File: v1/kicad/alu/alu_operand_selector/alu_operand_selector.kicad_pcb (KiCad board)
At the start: 2 copper layers, 166 x 91 mm, 19 parts, among them J1 LNCPU ALU Operand Selector so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, J10 OP_{out}, J2 A_{in}, J3 B_{in}, J4 C_{in}, J5 D_{in}, J6 E_{in}, J7 F_{in}, J8 G_{in}, J9 H_{in}, U1 74HC138, U2 74LS244, U3 74HC244, U4 74HC244, U5 74HC244, U6 74HC244, U7 74HC244, U8 74HC244, U9 74HC244

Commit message: partial
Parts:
- removed J1: LNCPU ALU Operand Selector socket, male, Connector_PinHeader_2.54mm:PinHeader_1x08_P2.54mm_Horizontal
- added U10: LNCPU Type C Connector, lncpu:LNCPU_Type_C_Header, F.Cu at (54.7, 75.4)
- U1: footprint Package_DIP:DIP-16_W7.62mm -> Package_DIP:DIP-16_W7.62mm_LongPads
- U2, U3, U4, U5, U6, U7, U8, U9: footprint Package_DIP:DIP-20_W7.62mm -> Package_DIP:DIP-20_W7.62mm_LongPads
- moved U1 11.5 mm to (65.6, 69.8)
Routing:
- net /OP_{out}5: track 320.6 -> 503.8 mm, vias 9 -> 10
- net Net-(J7-D4): track 45.5 -> 186.6 mm, vias 0 -> 2
- net /OP_{out}7: track 342.0 -> 457.8 mm, vias 9 -> 11
- net /EN.C: track 197.9 -> 84.0 mm, vias 6 -> 4
- net /OP_{out}2: track 311.4 -> 407.6 mm, vias 11 -> 10
- net /OP_{out}4: track 287.1 -> 380.0 mm, vias 7 -> 10
- net /OP_{out}0: track 294.9 -> 372.4 mm, vias 8 -> 11
- net /OP_{out}3: track 295.9 -> 370.0 mm, vias 9 -> 10
- net Net-(U1-VCC): track 364.0 -> 432.3 mm, vias 10 -> 9
- net /OP_{out}6: track 321.8 -> 384.8 mm, vias 9 -> 12
- net Net-(J2-D1): track 32.4 -> 93.1 mm, vias 0 -> 6
- net Net-(J2-D3): track 95.0 -> 38.0 mm, vias 2 -> 0
- net Net-(U1-GND): track 337.4 -> 377.2 mm, vias 9 -> 11
- net Net-(J8-D6): track 72.2 -> 33.2 mm
- net Net-(U1-A0): track 9.02 -> 42.4 mm, vias 0 -> 2
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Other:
- board size 166 x 91 mm -> 163.5 x 91 mm

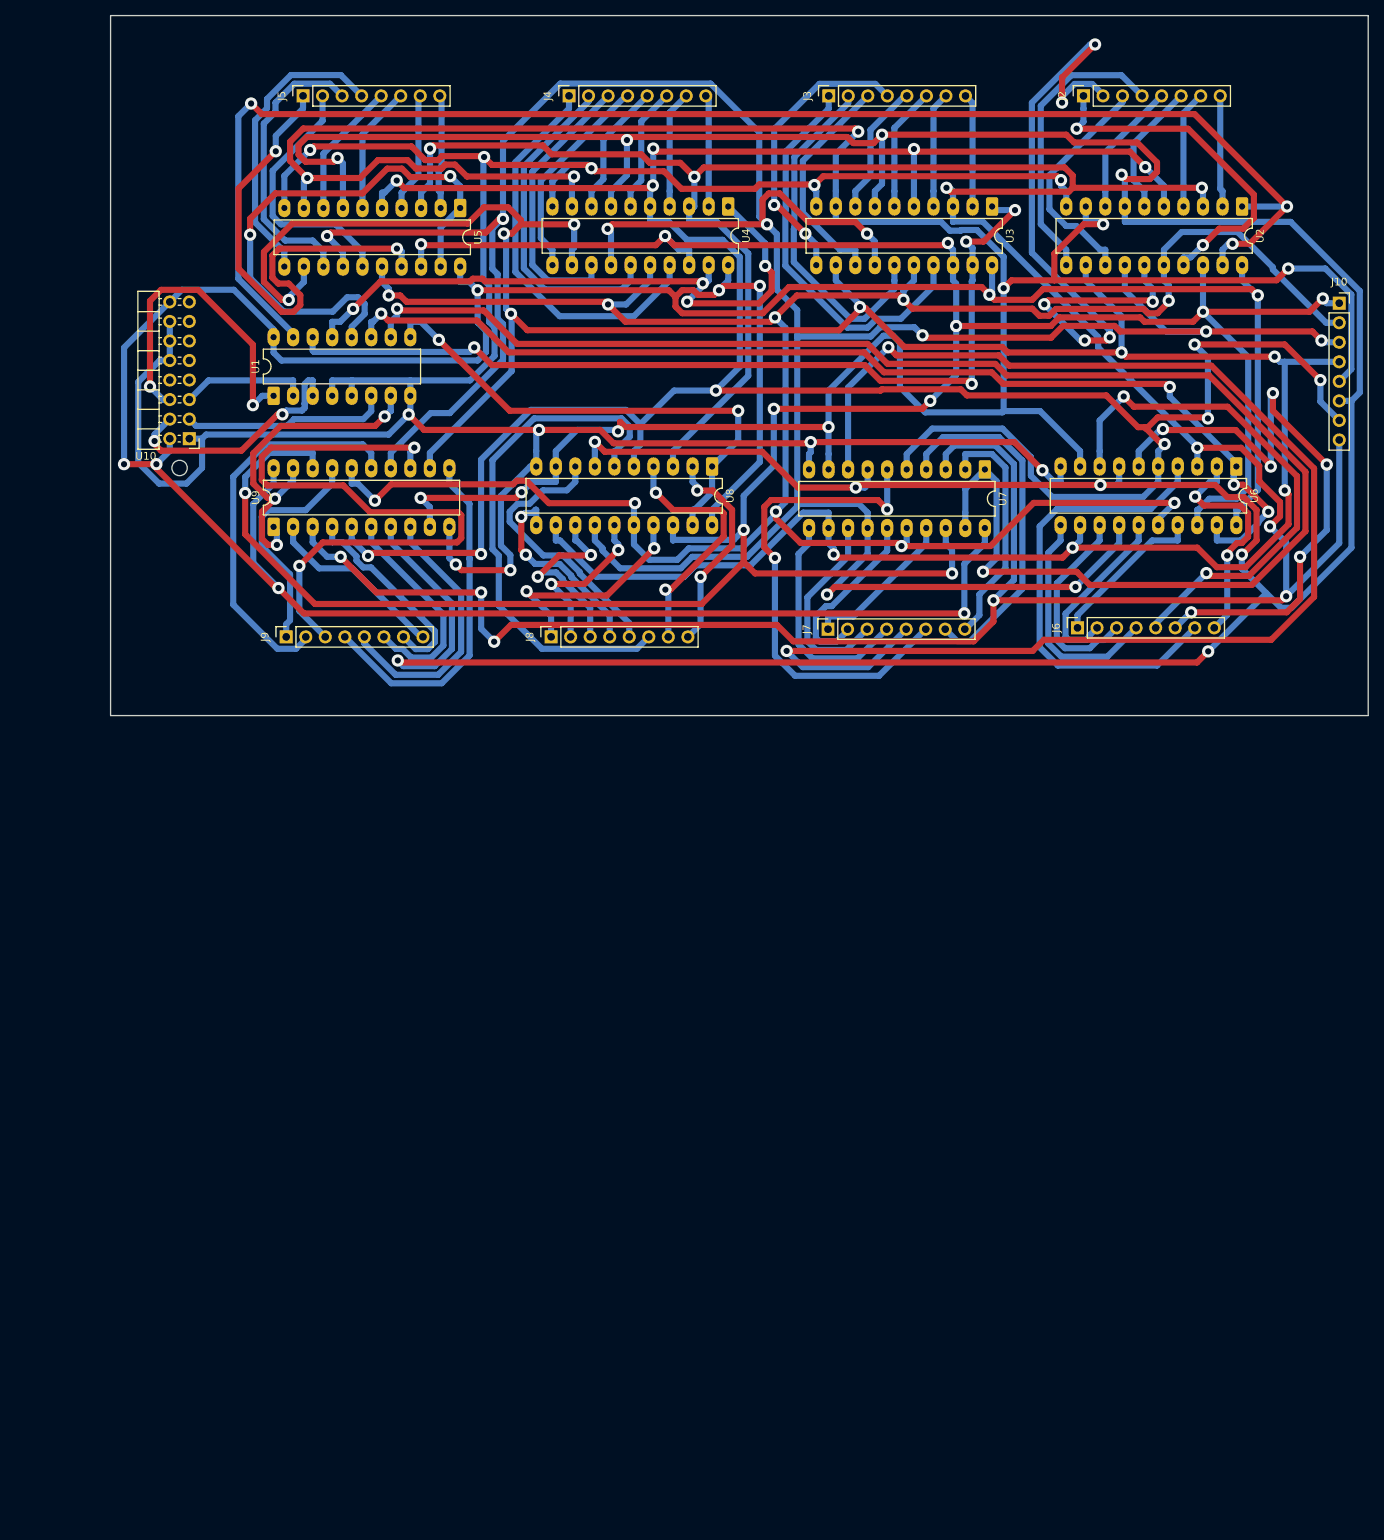
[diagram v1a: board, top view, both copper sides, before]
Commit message: readapt designs for BR, SP, SR, ALU
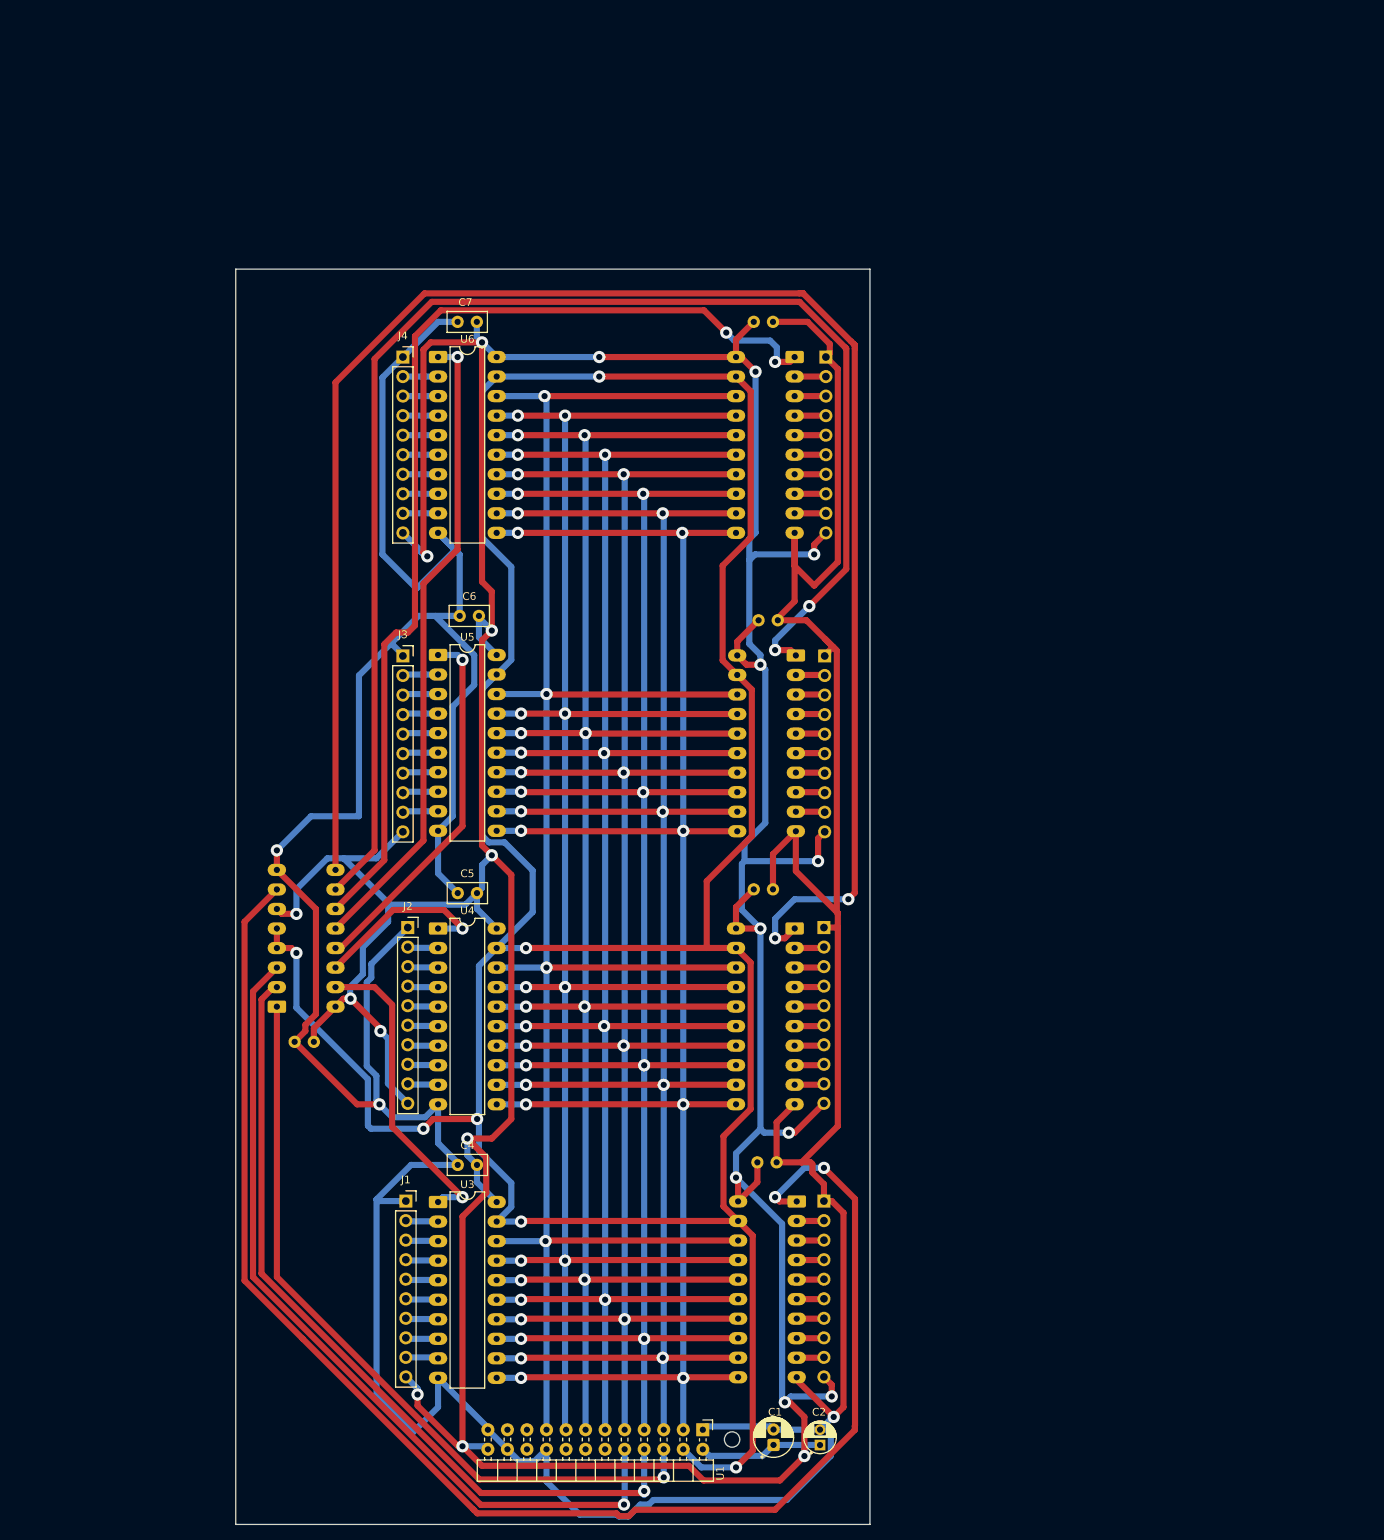
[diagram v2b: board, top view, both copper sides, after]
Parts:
- removed J10: OP_{out}, Connector_PinSocket_2.54mm:PinSocket_1x08_P2.54mm_Vertical
- removed J9: H_{in}, Connector_PinSocket_2.54mm:PinSocket_1x08_P2.54mm_Vertical
- added C1: 47u, Capacitor_THT:CP_Radial_D5.0mm_P2.00mm, F.Cu at (130.6, 206.2)
- added C10: 220n, Capacitor_THT:C_Disc_D5.0mm_W2.5mm_P2.50mm, B.Cu at (128.0, 134.0)
- added C11: 220n, Capacitor_THT:C_Disc_D5.0mm_W2.5mm_P2.50mm, B.Cu at (128.5, 169.5)
- added C2: 1u, lncpu:CP_Radial_D4.0mm_P2.00mm-Large-Holes, F.Cu at (136.7, 206.2)
- added C3: 100n, Capacitor_THT:C_Disc_D5.0mm_W2.5mm_P2.50mm, B.Cu at (70.8, 153.8)
- added C4: 220n, Capacitor_THT:C_Disc_D5.0mm_W2.5mm_P2.50mm, F.Cu at (92.1, 169.8)
- added C5: 220n, Capacitor_THT:C_Disc_D5.0mm_W2.5mm_P2.50mm, F.Cu at (92.1, 134.5)
- added C6: 220n, Capacitor_THT:C_Disc_D5.0mm_W2.5mm_P2.50mm, F.Cu at (92.3, 98.4)
- added C7: 220n, Capacitor_THT:C_Disc_D5.0mm_W2.5mm_P2.50mm, F.Cu at (92.0, 60.2)
- added C8: 220n, Capacitor_THT:C_Disc_D5.0mm_W2.5mm_P2.50mm, B.Cu at (128.0, 60.2)
- added C9: 220n, Capacitor_THT:C_Disc_D5.0mm_W2.5mm_P2.50mm, B.Cu at (128.7, 99.0)
- added J1: A_{in}, Connector_PinSocket_2.54mm:PinSocket_1x10_P2.54mm_Vertical, F.Cu at (82.8, 174.5)
- J2: value A_{in} -> B_{in}; footprint Connector_PinSocket_2.54mm:PinSocket_1x08_P2.54mm_Vertical -> Connector_PinSocket_2.54mm:PinSocket_1x10_P2.54mm_Vertical
- J3: value B_{in} -> C_{in}; footprint Connector_PinSocket_2.54mm:PinSocket_1x08_P2.54mm_Vertical -> Connector_PinSocket_2.54mm:PinSocket_1x10_P2.54mm_Vertical
- J4: value C_{in} -> D_{in}; footprint Connector_PinSocket_2.54mm:PinSocket_1x08_P2.54mm_Vertical -> Connector_PinSocket_2.54mm:PinSocket_1x10_P2.54mm_Vertical
- J5: value D_{in} -> E_{in}; footprint Connector_PinSocket_2.54mm:PinSocket_1x08_P2.54mm_Vertical -> Connector_PinSocket_2.54mm:PinSocket_1x10_P2.54mm_Vertical; moved to B.Cu
- J6: value E_{in} -> F_{in}; footprint Connector_PinSocket_2.54mm:PinSocket_1x08_P2.54mm_Vertical -> Connector_PinSocket_2.54mm:PinSocket_1x10_P2.54mm_Vertical; moved to B.Cu
- J7: value F_{in} -> G_{in}; footprint Connector_PinSocket_2.54mm:PinSocket_1x08_P2.54mm_Vertical -> Connector_PinSocket_2.54mm:PinSocket_1x10_P2.54mm_Vertical; moved to B.Cu
- J8: value G_{in} -> H_{in}; footprint Connector_PinSocket_2.54mm:PinSocket_1x08_P2.54mm_Vertical -> Connector_PinSocket_2.54mm:PinSocket_1x10_P2.54mm_Vertical; moved to B.Cu
- U1: value 74HC138 -> LNCPU Type B Header; footprint Package_DIP:DIP-16_W7.62mm_LongPads -> lncpu:LNCPU_Type_B_Header
- U10: value LNCPU Type C Connector -> 74HCT541; footprint lncpu:LNCPU_Type_C_Header -> Package_DIP:DIP-20_W7.62mm_LongPads; moved to B.Cu
- U2: value 74LS244 -> 74HC138; footprint Package_DIP:DIP-20_W7.62mm_LongPads -> Package_DIP:DIP-16_W7.62mm_LongPads; moved to B.Cu
- U3, U4, U5, U6: value 74HC244 -> 74HCT541
- U7, U8, U9: value 74HC244 -> 74HCT541; moved to B.Cu
- moved U2 163.0 mm to (66.0, 149.2), turned to 0 degrees
- moved U3 148.1 mm to (87.0, 174.6), turned to 0 degrees
- moved U1 145.5 mm to (121.4, 204.2), turned to -90 degrees
- moved J2 139.3 mm to (83.1, 138.9), turned to 0 degrees
- moved U10 126.8 mm to (133.6, 174.5)
- moved U6 104.8 mm to (87.0, 64.8), turned to 0 degrees
- moved U4 101.2 mm to (87.0, 139.1), turned to 0 degrees
- moved J3 91.5 mm to (82.4, 103.6), turned to 0 degrees
- moved U9 85.5 mm to (133.3, 139.1), turned to 180 degrees
- moved J8 81.5 mm to (137.2, 174.5), turned to 180 degrees
- moved J5 76.0 mm to (137.4, 64.8), turned to 180 degrees
- moved U5 58.2 mm to (87.0, 103.5), turned to 0 degrees
- moved J4 40.2 mm to (82.4, 64.8), turned to 0 degrees
- moved J7 38.8 mm to (137.2, 138.9), turned to 180 degrees
- moved J6 33.1 mm to (137.3, 103.6), turned to 180 degrees
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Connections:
- J2 pad 1: Net-(J2-D0) -> Net-(J1-GND)
- J2 pad 2: Net-(J2-D1) -> Net-(J2-D0)
- J2 pad 3: Net-(J2-D2) -> Net-(J2-D1)
- J2 pad 4: Net-(J2-D3) -> Net-(J2-D2)
- J2 pad 5: Net-(J2-D4) -> Net-(J2-D3)
- J2 pad 6: Net-(J2-D5) -> Net-(J2-D4)
- J2 pad 7: Net-(J2-D6) -> Net-(J2-D5)
- J2 pad 8: Net-(J2-D7) -> Net-(J2-D6)
- J3 pad 1: Net-(J3-D0) -> Net-(J1-GND)
- J3 pad 2: Net-(J3-D1) -> Net-(J3-D0)
- J3 pad 3: Net-(J3-D2) -> Net-(J3-D1)
- J3 pad 4: Net-(J3-D3) -> Net-(J3-D2)
- J3 pad 5: Net-(J3-D4) -> Net-(J3-D3)
- J3 pad 6: Net-(J3-D5) -> Net-(J3-D4)
- J3 pad 7: Net-(J3-D6) -> Net-(J3-D5)
- J3 pad 8: Net-(J3-D7) -> Net-(J3-D6)
- J4 pad 1: Net-(J4-D0) -> Net-(J1-GND)
- J4 pad 2: Net-(J4-D1) -> Net-(J4-D0)
- J4 pad 3: Net-(J4-D2) -> Net-(J4-D1)
- J4 pad 4: Net-(J4-D3) -> Net-(J4-D2)
- J4 pad 5: Net-(J4-D4) -> Net-(J4-D3)
- J4 pad 6: Net-(J4-D5) -> Net-(J4-D4)
- J4 pad 7: Net-(J4-D6) -> Net-(J4-D5)
- J4 pad 8: Net-(J4-D7) -> Net-(J4-D6)
- J5 pad 1: Net-(J5-D0) -> Net-(J1-GND)
- J5 pad 2: Net-(J5-D1) -> Net-(J5-D0)
- J5 pad 3: Net-(J5-D2) -> Net-(J5-D1)
- J5 pad 4: Net-(J5-D3) -> Net-(J5-D2)
- J5 pad 5: Net-(J5-D4) -> Net-(J5-D3)
- J5 pad 6: Net-(J5-D5) -> Net-(J5-D4)
- J5 pad 7: Net-(J5-D6) -> Net-(J5-D5)
- J5 pad 8: Net-(J5-D7) -> Net-(J5-D6)
- J6 pad 1: Net-(J6-D0) -> Net-(J1-GND)
- J6 pad 2: Net-(J6-D1) -> Net-(J6-D0)
- J6 pad 3: Net-(J6-D2) -> Net-(J6-D1)
- J6 pad 4: Net-(J6-D3) -> Net-(J6-D2)
- J6 pad 5: Net-(J6-D4) -> Net-(J6-D3)
- J6 pad 6: Net-(J6-D5) -> Net-(J6-D4)
- J6 pad 7: Net-(J6-D6) -> Net-(J6-D5)
- J6 pad 8: Net-(J6-D7) -> Net-(J6-D6)
- J7 pad 1: Net-(J7-D0) -> Net-(J1-GND)
- J7 pad 2: Net-(J7-D1) -> Net-(J7-D0)
- J7 pad 3: Net-(J7-D2) -> Net-(J7-D1)
- J7 pad 4: Net-(J7-D3) -> Net-(J7-D2)
- J7 pad 5: Net-(J7-D4) -> Net-(J7-D3)
- J7 pad 6: Net-(J7-D5) -> Net-(J7-D4)
- J7 pad 7: Net-(J7-D6) -> Net-(J7-D5)
- J7 pad 8: Net-(J7-D7) -> Net-(J7-D6)
- J8 pad 1: Net-(J8-D0) -> Net-(J1-GND)
- J8 pad 2: Net-(J8-D1) -> Net-(J8-D0)
- J8 pad 3: Net-(J8-D2) -> Net-(J8-D1)
- J8 pad 4: Net-(J8-D3) -> Net-(J8-D2)
- J8 pad 5: Net-(J8-D4) -> Net-(J8-D3)
- J8 pad 6: Net-(J8-D5) -> Net-(J8-D4)
- J8 pad 7: Net-(J8-D6) -> Net-(J8-D5)
- J8 pad 8: Net-(J8-D7) -> Net-(J8-D6)
- U1 pad 1: Net-(U1-A0) -> Net-(J1-GND)
- U1 pad 10: /EN.F -> Net-(U1-CTRL_{3})
- U1 pad 11: /EN.E -> /OP_{out}3
- U1 pad 12: /EN.D -> unconnected-(U1-CTRL_{4}-Pad12)
- U1 pad 13: /EN.C -> /OP_{out}2
- U1 pad 14: /EN.B -> unconnected-(U1-CTRL_{5}-Pad14)
- U1 pad 15: /EN.A -> /OP_{out}1
- U1 pad 16: Net-(U1-VCC) -> unconnected-(U1-CTRL_{6}-Pad16)
- U1 pad 2: Net-(U1-A1) -> Net-(J1-VCC)
- U1 pad 3: Net-(U1-A2) -> /OP_{out}7
- U1 pad 4: Net-(U1-GND) -> /~{EN}
- U1 pad 5: Net-(U1-GND) -> /OP_{out}6
- U1 pad 6: Net-(U1-E3) -> Net-(U1-CTRL_{1})
- U1 pad 7: /EN.H -> /OP_{out}5
- U1 pad 8: Net-(U1-GND) -> Net-(U1-CTRL_{2})
- U1 pad 9: /EN.G -> /OP_{out}4
- U10 pad 1: Net-(U1-GND) -> /EN.H
- U10 pad 10: Net-(U1-GND) -> Net-(J1-GND)
- U10 pad 11: unconnected-(U10-RST-Pad11) -> /OP_{out}7
- U10 pad 12: Net-(U1-GND) -> /OP_{out}6
- U10 pad 13: unconnected-(U10-CLK1-Pad13) -> /OP_{out}5
- U10 pad 14: Net-(U1-GND) -> /OP_{out}4
- U10 pad 15: unconnected-(U10-CLK2-Pad15) -> /OP_{out}3
- U10 pad 16: Net-(U1-VCC) -> /OP_{out}2
- U10 pad 2: Net-(U1-VCC) -> Net-(J8-D0)
- U10 pad 3: Net-(U1-E3) -> Net-(J8-D1)
- U10 pad 4: Net-(U1-A2) -> Net-(J8-D2)
- U10 pad 5: Net-(U1-A1) -> Net-(J8-D3)
- U10 pad 6: Net-(U1-A0) -> Net-(J8-D4)
- U10 pad 7: unconnected-(U10-CTRL_{4}-Pad7) -> Net-(J8-D5)
- U10 pad 8: unconnected-(U10-CTRL_{5}-Pad8) -> Net-(J8-D6)
- U10 pad 9: unconnected-(U10-CTRL_{6}-Pad9) -> Net-(J8-D7)
- U2 pad 1: /EN.A -> Net-(U1-CTRL_{1})
- U2 pad 10: Net-(U1-GND) -> /EN.F
- U2 pad 11: Net-(J2-D3) -> /EN.E
- U2 pad 12: /OP_{out}3 -> /EN.D
- U2 pad 13: Net-(J2-D2) -> /EN.C
- U2 pad 14: /OP_{out}2 -> /EN.B
- U2 pad 15: Net-(J2-D1) -> /EN.A
- U2 pad 16: /OP_{out}1 -> Net-(J1-VCC)
- U2 pad 2: Net-(J2-D7) -> Net-(U1-CTRL_{2})
- U2 pad 3: /OP_{out}7 -> Net-(U1-CTRL_{3})
- U2 pad 4: Net-(J2-D6) -> /~{EN}
- U2 pad 5: /OP_{out}6 -> /~{EN}
- U2 pad 6: Net-(J2-D5) -> Net-(J1-VCC)
- U2 pad 7: /OP_{out}5 -> /EN.H
- U2 pad 8: Net-(J2-D4) -> Net-(J1-GND)
- U2 pad 9: /OP_{out}4 -> /EN.G
- U3 pad 1: /EN.B -> /EN.A
- U3 pad 10: Net-(U1-GND) -> Net-(J1-GND)
- U3 pad 11: Net-(J3-D3) -> /OP_{out}7
- U3 pad 12: /OP_{out}3 -> /OP_{out}6
- U3 pad 13: Net-(J3-D2) -> /OP_{out}5
- U3 pad 14: /OP_{out}2 -> /OP_{out}4
- U3 pad 15: Net-(J3-D1) -> /OP_{out}3
- U3 pad 16: /OP_{out}1 -> /OP_{out}2
- U3 pad 17: Net-(J3-D0) -> /OP_{out}1
- U3 pad 19: /EN.B -> /~{EN}
- U3 pad 2: Net-(J3-D7) -> Net-(J1-D0)
- U3 pad 20: Net-(U1-VCC) -> Net-(J1-VCC)
- U3 pad 3: /OP_{out}7 -> Net-(J1-D1)
- U3 pad 4: Net-(J3-D6) -> Net-(J1-D2)
- U3 pad 5: /OP_{out}6 -> Net-(J1-D3)
- U3 pad 6: Net-(J3-D5) -> Net-(J1-D4)
- U3 pad 7: /OP_{out}5 -> Net-(J1-D5)
- U3 pad 8: Net-(J3-D4) -> Net-(J1-D6)
- U3 pad 9: /OP_{out}4 -> Net-(J1-D7)
- U4 pad 1: /EN.C -> /EN.B
- U4 pad 10: Net-(U1-GND) -> Net-(J1-GND)
- U4 pad 11: Net-(J4-D3) -> /OP_{out}7
- U4 pad 12: /OP_{out}3 -> /OP_{out}6
- U4 pad 13: Net-(J4-D2) -> /OP_{out}5
- U4 pad 14: /OP_{out}2 -> /OP_{out}4
- U4 pad 15: Net-(J4-D1) -> /OP_{out}3
- U4 pad 16: /OP_{out}1 -> /OP_{out}2
- U4 pad 17: Net-(J4-D0) -> /OP_{out}1
- U4 pad 19: /EN.C -> /~{EN}
- U4 pad 2: Net-(J4-D7) -> Net-(J2-D0)
- U4 pad 20: Net-(U1-VCC) -> Net-(J1-VCC)
- U4 pad 3: /OP_{out}7 -> Net-(J2-D1)
- U4 pad 4: Net-(J4-D6) -> Net-(J2-D2)
- U4 pad 5: /OP_{out}6 -> Net-(J2-D3)
- U4 pad 6: Net-(J4-D5) -> Net-(J2-D4)
- U4 pad 7: /OP_{out}5 -> Net-(J2-D5)
- U4 pad 8: Net-(J4-D4) -> Net-(J2-D6)
- U4 pad 9: /OP_{out}4 -> Net-(J2-D7)
- U5 pad 1: /EN.D -> /EN.C
- U5 pad 10: Net-(U1-GND) -> Net-(J1-GND)
- U5 pad 11: Net-(J5-D3) -> /OP_{out}7
- U5 pad 12: /OP_{out}3 -> /OP_{out}6
- U5 pad 13: Net-(J5-D2) -> /OP_{out}5
- U5 pad 14: /OP_{out}2 -> /OP_{out}4
- U5 pad 15: Net-(J5-D1) -> /OP_{out}3
- U5 pad 16: /OP_{out}1 -> /OP_{out}2
- U5 pad 17: Net-(J5-D0) -> /OP_{out}1
- U5 pad 19: /EN.D -> /~{EN}
- U5 pad 2: Net-(J5-D7) -> Net-(J3-D0)
- U5 pad 20: Net-(U1-VCC) -> Net-(J1-VCC)
- U5 pad 3: /OP_{out}7 -> Net-(J3-D1)
- U5 pad 4: Net-(J5-D6) -> Net-(J3-D2)
- U5 pad 5: /OP_{out}6 -> Net-(J3-D3)
- U5 pad 6: Net-(J5-D5) -> Net-(J3-D4)
- U5 pad 7: /OP_{out}5 -> Net-(J3-D5)
- U5 pad 8: Net-(J5-D4) -> Net-(J3-D6)
- U5 pad 9: /OP_{out}4 -> Net-(J3-D7)
- U6 pad 1: /EN.E -> /EN.D
- U6 pad 10: Net-(U1-GND) -> Net-(J1-GND)
- U6 pad 11: Net-(J6-D3) -> /OP_{out}7
- U6 pad 12: /OP_{out}3 -> /OP_{out}6
- U6 pad 13: Net-(J6-D2) -> /OP_{out}5
- U6 pad 14: /OP_{out}2 -> /OP_{out}4
- U6 pad 15: Net-(J6-D1) -> /OP_{out}3
- U6 pad 16: /OP_{out}1 -> /OP_{out}2
- U6 pad 17: Net-(J6-D0) -> /OP_{out}1
- U6 pad 19: /EN.E -> /~{EN}
- U6 pad 2: Net-(J6-D7) -> Net-(J4-D0)
- U6 pad 20: Net-(U1-VCC) -> Net-(J1-VCC)
- U6 pad 3: /OP_{out}7 -> Net-(J4-D1)
- U6 pad 4: Net-(J6-D6) -> Net-(J4-D2)
- U6 pad 5: /OP_{out}6 -> Net-(J4-D3)
- U6 pad 6: Net-(J6-D5) -> Net-(J4-D4)
- U6 pad 7: /OP_{out}5 -> Net-(J4-D5)
- U6 pad 8: Net-(J6-D4) -> Net-(J4-D6)
- U6 pad 9: /OP_{out}4 -> Net-(J4-D7)
- U7 pad 1: /EN.F -> /EN.E
- U7 pad 10: Net-(U1-GND) -> Net-(J1-GND)
- U7 pad 11: Net-(J7-D3) -> /OP_{out}7
- U7 pad 12: /OP_{out}3 -> /OP_{out}6
- U7 pad 13: Net-(J7-D2) -> /OP_{out}5
- U7 pad 14: /OP_{out}2 -> /OP_{out}4
- U7 pad 15: Net-(J7-D1) -> /OP_{out}3
- U7 pad 16: /OP_{out}1 -> /OP_{out}2
- U7 pad 17: Net-(J7-D0) -> /OP_{out}1
- U7 pad 19: /EN.F -> /~{EN}
- U7 pad 2: Net-(J7-D7) -> Net-(J5-D0)
- U7 pad 20: Net-(U1-VCC) -> Net-(J1-VCC)
- U7 pad 3: /OP_{out}7 -> Net-(J5-D1)
- U7 pad 4: Net-(J7-D6) -> Net-(J5-D2)
- U7 pad 5: /OP_{out}6 -> Net-(J5-D3)
- U7 pad 6: Net-(J7-D5) -> Net-(J5-D4)
- U7 pad 7: /OP_{out}5 -> Net-(J5-D5)
- U7 pad 8: Net-(J7-D4) -> Net-(J5-D6)
- U7 pad 9: /OP_{out}4 -> Net-(J5-D7)
- U8 pad 1: /EN.G -> /EN.F
- U8 pad 10: Net-(U1-GND) -> Net-(J1-GND)
- U8 pad 11: Net-(J8-D3) -> /OP_{out}7
- U8 pad 12: /OP_{out}3 -> /OP_{out}6
- U8 pad 13: Net-(J8-D2) -> /OP_{out}5
- U8 pad 14: /OP_{out}2 -> /OP_{out}4
- U8 pad 15: Net-(J8-D1) -> /OP_{out}3
- U8 pad 16: /OP_{out}1 -> /OP_{out}2
- U8 pad 17: Net-(J8-D0) -> /OP_{out}1
- U8 pad 19: /EN.G -> /~{EN}
- U8 pad 2: Net-(J8-D7) -> Net-(J6-D0)
- U8 pad 20: Net-(U1-VCC) -> Net-(J1-VCC)
- U8 pad 3: /OP_{out}7 -> Net-(J6-D1)
- U8 pad 4: Net-(J8-D6) -> Net-(J6-D2)
- U8 pad 5: /OP_{out}6 -> Net-(J6-D3)
- U8 pad 6: Net-(J8-D5) -> Net-(J6-D4)
- U8 pad 7: /OP_{out}5 -> Net-(J6-D5)
- U8 pad 8: Net-(J8-D4) -> Net-(J6-D6)
- U8 pad 9: /OP_{out}4 -> Net-(J6-D7)
- U9 pad 1: /EN.H -> /EN.G
- U9 pad 10: Net-(U1-GND) -> Net-(J1-GND)
- U9 pad 11: Net-(J9-D3) -> /OP_{out}7
- U9 pad 12: /OP_{out}3 -> /OP_{out}6
- U9 pad 13: Net-(J9-D2) -> /OP_{out}5
- U9 pad 14: /OP_{out}2 -> /OP_{out}4
- U9 pad 15: Net-(J9-D1) -> /OP_{out}3
- U9 pad 16: /OP_{out}1 -> /OP_{out}2
- U9 pad 17: Net-(J9-D0) -> /OP_{out}1
- U9 pad 19: /EN.H -> /~{EN}
- U9 pad 2: Net-(J9-D7) -> Net-(J7-D0)
- U9 pad 20: Net-(U1-VCC) -> Net-(J1-VCC)
- U9 pad 3: /OP_{out}7 -> Net-(J7-D1)
- U9 pad 4: Net-(J9-D6) -> Net-(J7-D2)
- U9 pad 5: /OP_{out}6 -> Net-(J7-D3)
- U9 pad 6: Net-(J9-D5) -> Net-(J7-D4)
- U9 pad 7: /OP_{out}5 -> Net-(J7-D5)
- U9 pad 8: Net-(J9-D4) -> Net-(J7-D6)
- U9 pad 9: /OP_{out}4 -> Net-(J7-D7)
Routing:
- net Net-(J1-VCC): track 0.00 -> 654.9 mm, vias 0 -> 21
- net Net-(J1-GND): track 0.00 -> 610.6 mm, vias 0 -> 3
- net Net-(U1-VCC): track 432.3 -> 0.00 mm, vias 9 -> 0
- net /~{EN}: track 0.00 -> 424.0 mm, vias 0 -> 7
- net Net-(U1-GND): track 377.2 -> 0.00 mm, vias 11 -> 0
- net /OP_{out}5: track 503.8 -> 246.7 mm, vias 10 -> 8
- net /OP_{out}7: track 457.8 -> 241.6 mm, vias 11 -> 8
- net Net-(J7-D4): track 186.6 -> 4.06 mm, vias 2 -> 0
- net /EN.G: track 66.9 -> 227.0 mm
- net /OP_{out}2: track 407.6 -> 254.0 mm, vias 10 -> 8
- net /EN.A: track 192.9 -> 40.6 mm, vias 3 -> 1
- net /EN.H: track 45.6 -> 196.0 mm, vias 3 -> 2
- net /OP_{out}6: track 384.8 -> 244.0 mm, vias 12 -> 8
- net /OP_{out}4: track 380.0 -> 249.2 mm, vias 10 -> 8
- net /OP_{out}3: track 370.0 -> 251.8 mm, vias 10 -> 8
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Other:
- board size 163.5 x 91 mm -> 82.5 x 163.2 mm
